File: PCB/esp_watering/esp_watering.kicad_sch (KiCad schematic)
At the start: 33 parts, among them J1 Zone 0, J10 Zone 9, J11 Zone 10, J12 Zone 11, J13 Zone 12, J14 Zone 13, J15 Zone 14, J16 Zone 15, J17 Zone 16, J18 Zone 17, J19 Zone 18, J2 Zone 1, J20 Zone 19, J21 Flow_Sensor, J22 +12V_In, J23 +5V_In, J3 Zone 2, J4 Zone 3, J5 Zone 4, J6 Zone 5, J7 Zone 6, J8 Zone 7, J9 Zone 8, U1 ESP32-DevKit, U2 SN74HC595_1, U3 SN74HC595_2, U4 SN74HC595_3, U5 ULN2003_1, U6 ULN2003_2, U7 ULN2003_3, U8 SSD1306_128x64

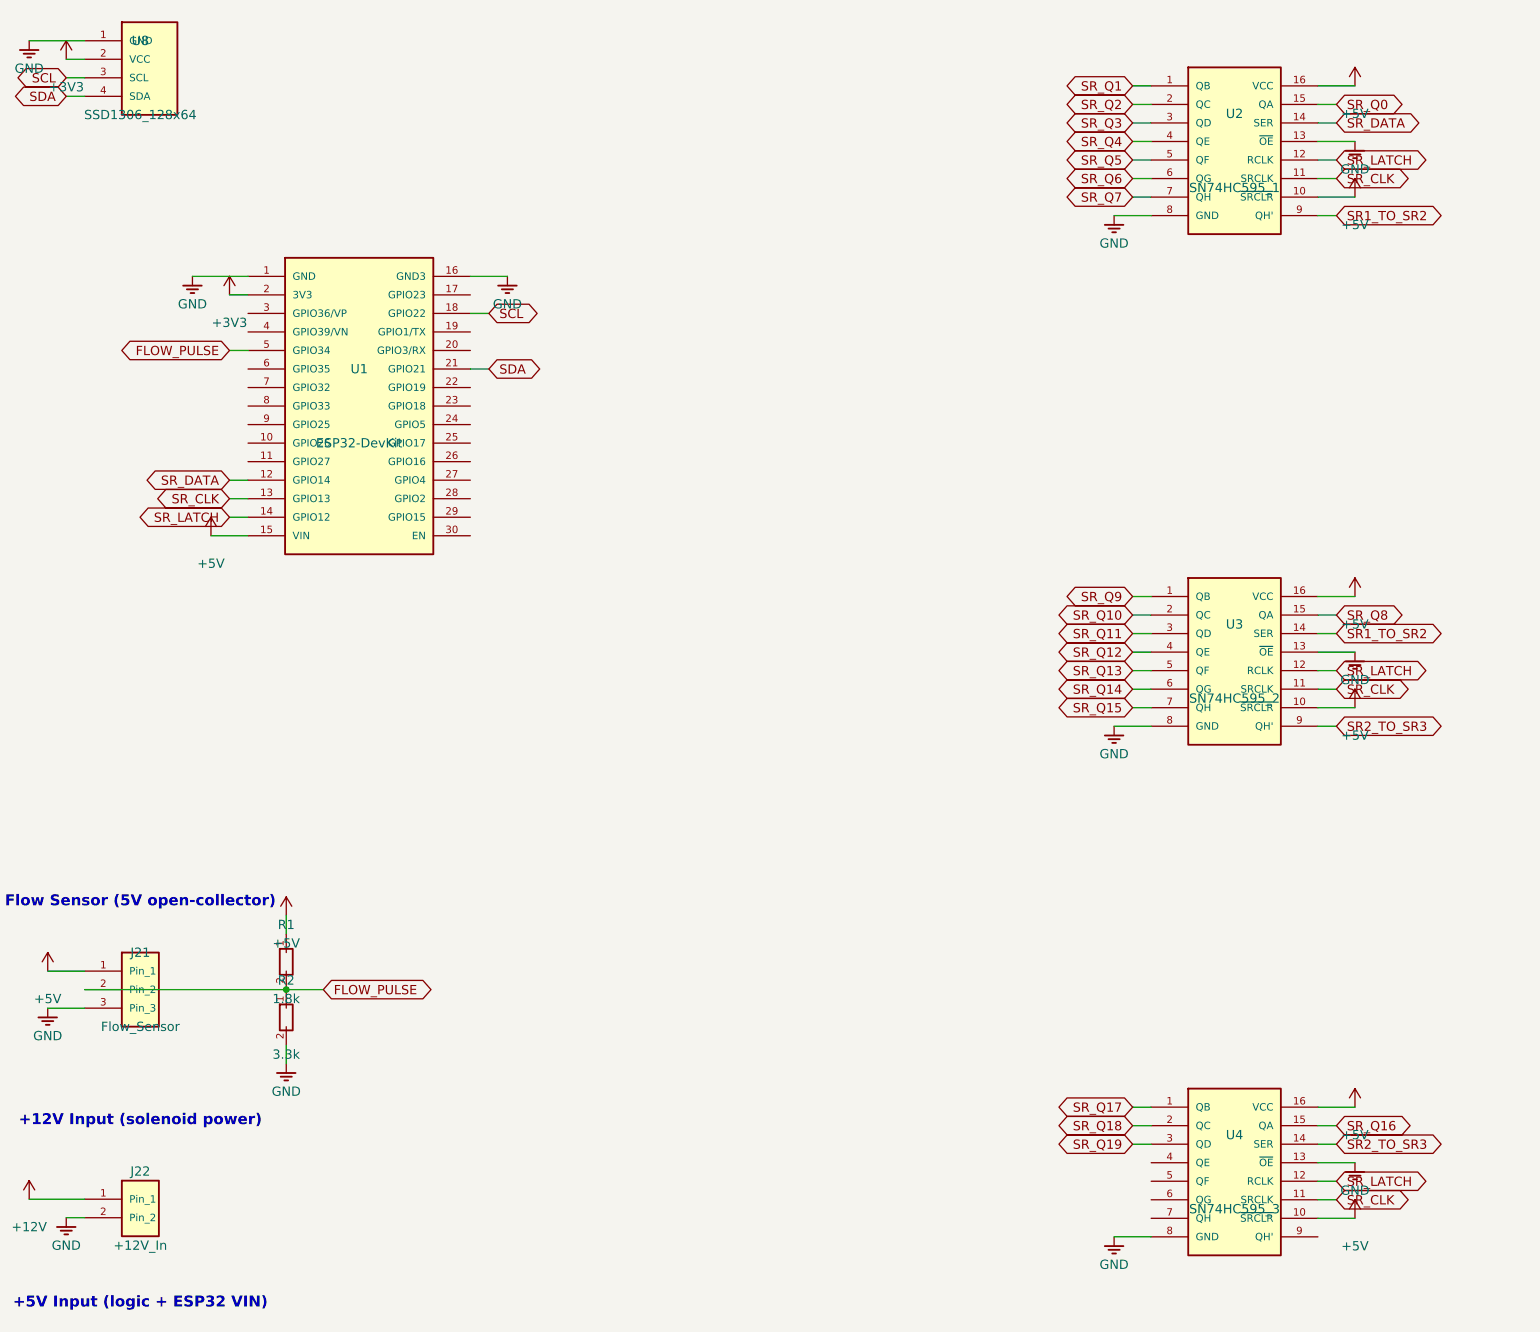
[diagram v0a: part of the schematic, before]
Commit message: PCB: remap SR pins, route /OE through GPIO16 + 10k pull-up
generate_schematic.py: SHIFT_REG_DATA/CLOCK/LATCH now GPIO23/18/5, new
SHIFT_REG_OE = GPIO16. Replaces the GND-tied /OE on each SN74HC595 with
a SR_OE net driven by ESP32 GPIO16 (open-drain) and pulled up to +5V by
a new 10k resistor R3. /OE stays high through ESP32 reset / boot, so
the SRs cannot energize valves on garbage contents.
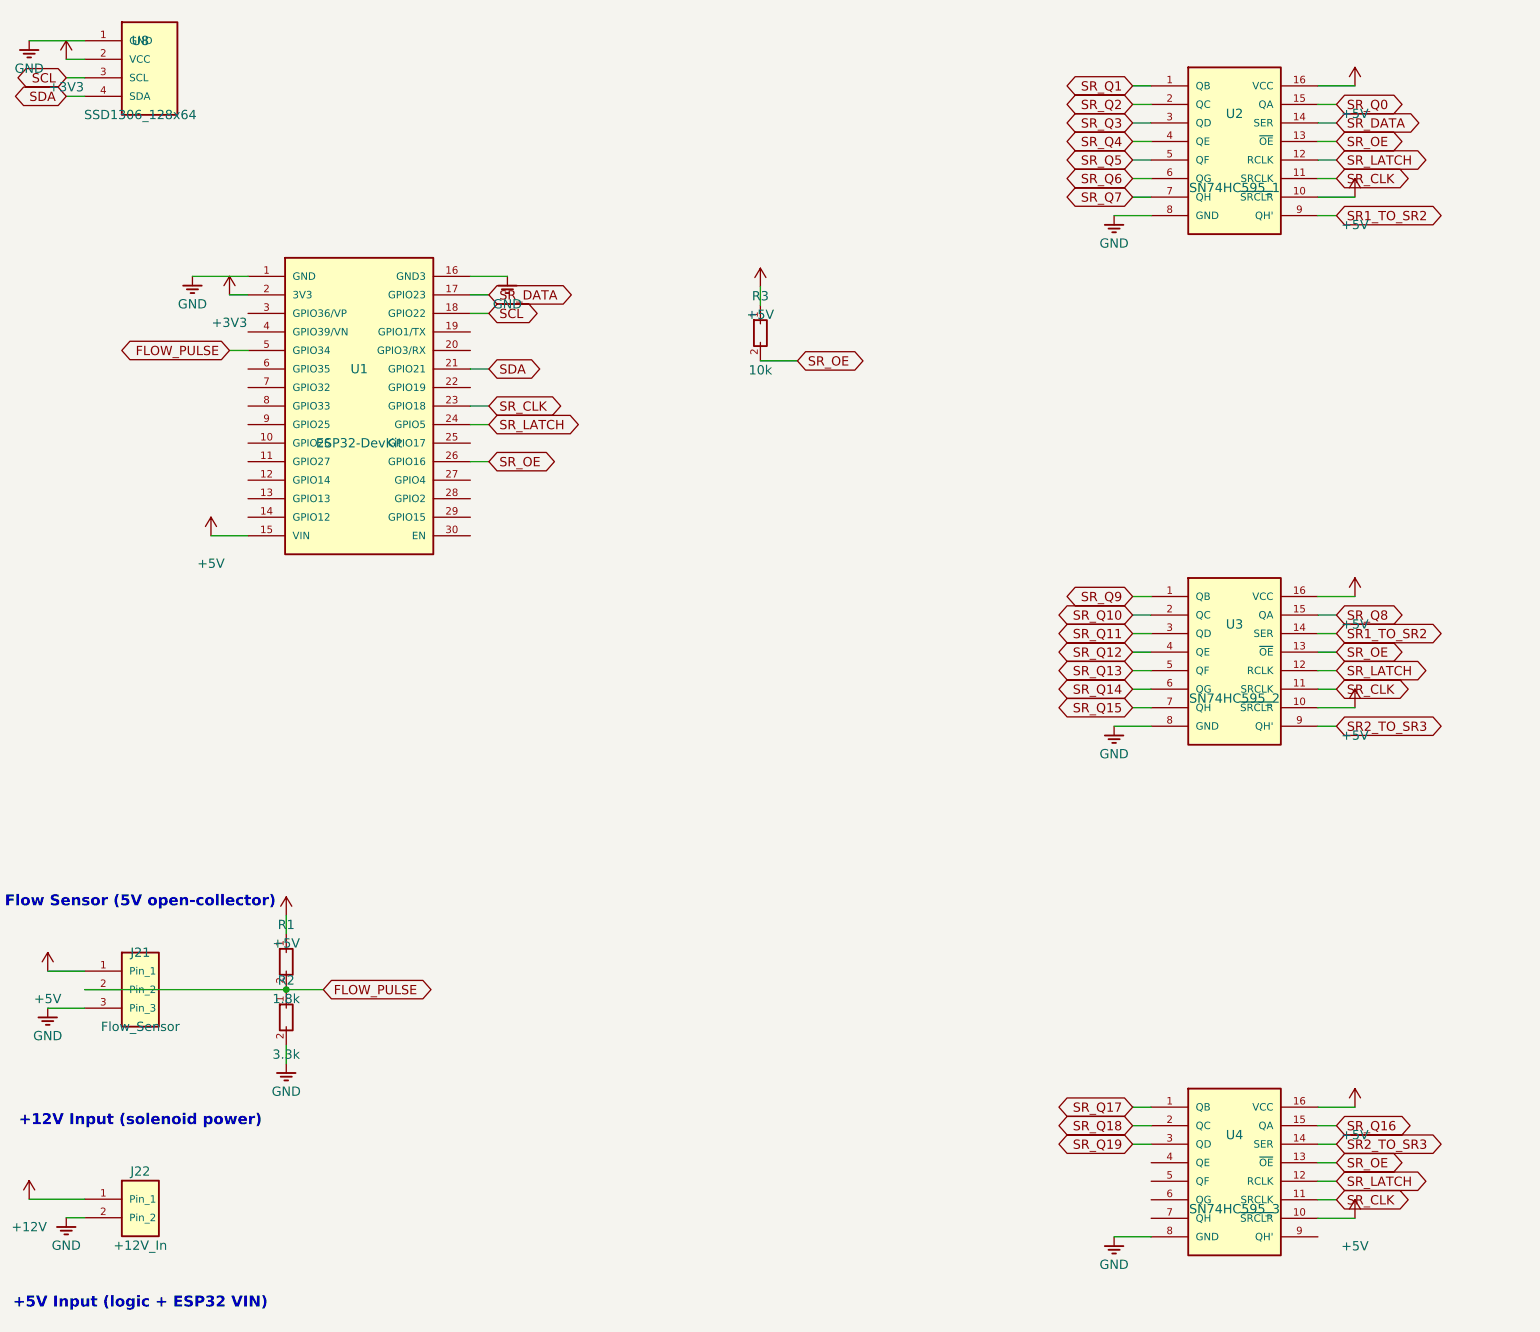
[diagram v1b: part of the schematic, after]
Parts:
- added R3: 10k, symbol irrigation:R
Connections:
- net +5V: now also R3.1
- net GND: no longer U2.13 (~{OE}), U3.13 (~{OE}), U4.13 (~{OE})
- net SR_CLK: now also U1.23 (GPIO18); no longer U1.13 (GPIO13)
- net SR_DATA: now also U1.17 (GPIO23); no longer U1.12 (GPIO14)
- net SR_LATCH: now also U1.24 (GPIO5); no longer U1.14 (GPIO12)
- net SR_OE: now reaches U1.26 (GPIO16)
- net SR_OE: now also U2.13 (~{OE}), U3.13 (~{OE}), U4.13 (~{OE}), R3.2

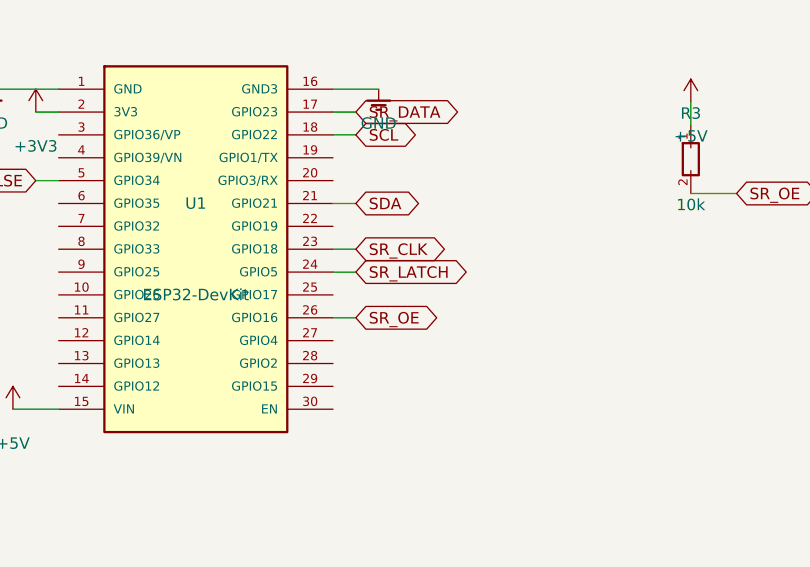
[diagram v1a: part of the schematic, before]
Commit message: Move SR latch from GPIO5 to GPIO17
GPIO5 is listed in the ESP32 GPIO reference as a "PWM output at boot"
pin (along with 1, 3, 14, 15) — the bootloader briefly toggles it.
/OE held high already neutralizes that, but GPIO17 is unambiguously
safe at boot (no strapping, no boot pulses), so use it instead.
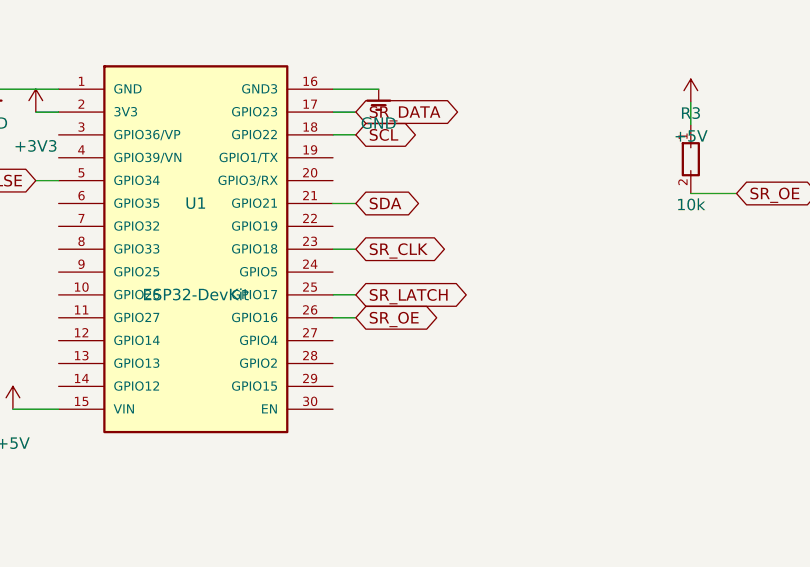
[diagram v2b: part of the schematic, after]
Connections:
- net SR_LATCH: now also U1.25 (GPIO17); no longer U1.24 (GPIO5)
